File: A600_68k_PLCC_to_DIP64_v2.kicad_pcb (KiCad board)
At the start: 4 copper layers, 101.9 x 69.8 mm, 16 parts, among them J1 171826-4, U1 MC68000_PLCC68, U2 68000_SOCKET

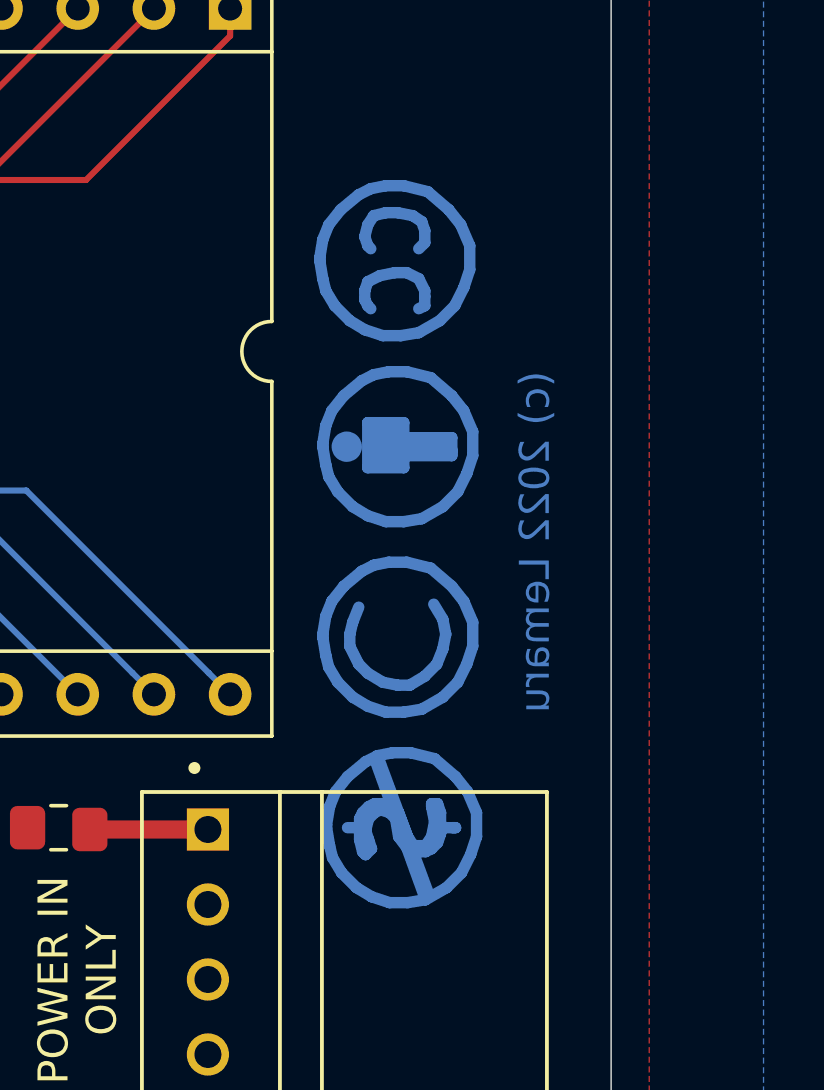
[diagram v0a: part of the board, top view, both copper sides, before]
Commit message: Tweaked silk screen and updated gerbers
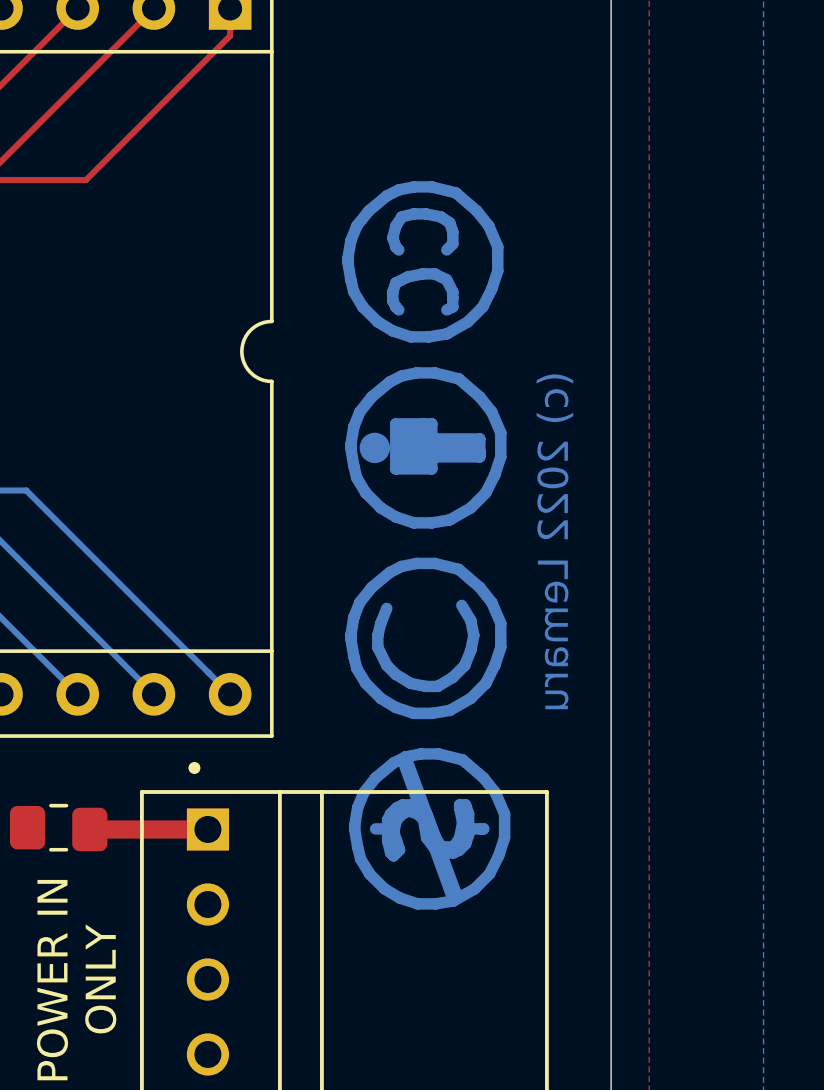
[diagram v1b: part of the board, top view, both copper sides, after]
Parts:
- moved REF** 0.94 mm to (202.2, 108.6)
- moved REF** 0.94 mm to (202.1, 89.6)
- moved REF** 0.94 mm to (202.1, 102.3)
- moved REF** 0.94 mm to (202.1, 95.9)
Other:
- board text added: "+5V"
- board text added: "GND"
- board text added: "N/C"

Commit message: Added GND vias, and corrected cap values
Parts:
- removed REF**: Symbol_CC-Noncommercial_CopperTop_Small, Symbol:Symbol_CC-Noncommercial_CopperTop_Small
- removed REF**: Symbol_CC-ShareAlike_CopperTop_Small, Symbol:Symbol_CC-ShareAlike_CopperTop_Small
- removed REF**: Symbol_CC-Attribution_CopperTop_Small, Symbol:Symbol_CC-Attribution_CopperTop_Small
- removed REF**: Symbol_CreativeCommons_CopperTop_Type2_Small, Symbol:Symbol_CreativeCommons_CopperTop_Type2_Small
- C1, C2, C3, C4, C5: value 100nf -> 10uf
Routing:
- net GND: vias 0 -> 6
